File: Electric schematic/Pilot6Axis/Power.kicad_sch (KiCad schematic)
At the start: 14 parts, among them IC1 LM27313XMFX_NOPB, J1 Power switch, U1 AMS1117-3.3

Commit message: update schematic to kicajd 9.0,    fixed usb D=/D- wrongly inerconnected , otherwise pcb seems to be woekring
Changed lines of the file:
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@@
 (kicad_sch
-	(version 20231120)
+	(version 20250114)
 	(generator "eeschema")
-	(generator_version "8.0")
+	(generator_version "9.0")
 	(paper "A4")
 	(junction

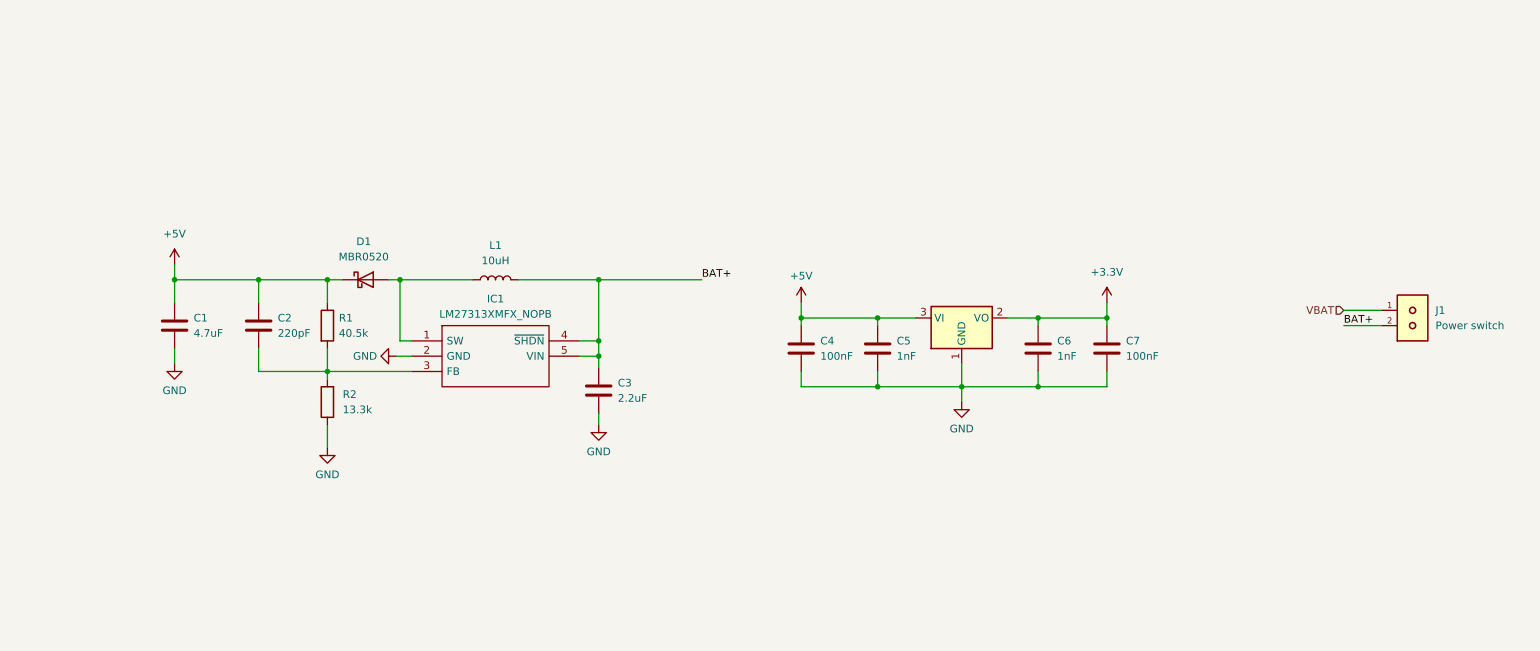
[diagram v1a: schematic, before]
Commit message: upgrade board to use USB BD for power delivery and addded SPI screen conector
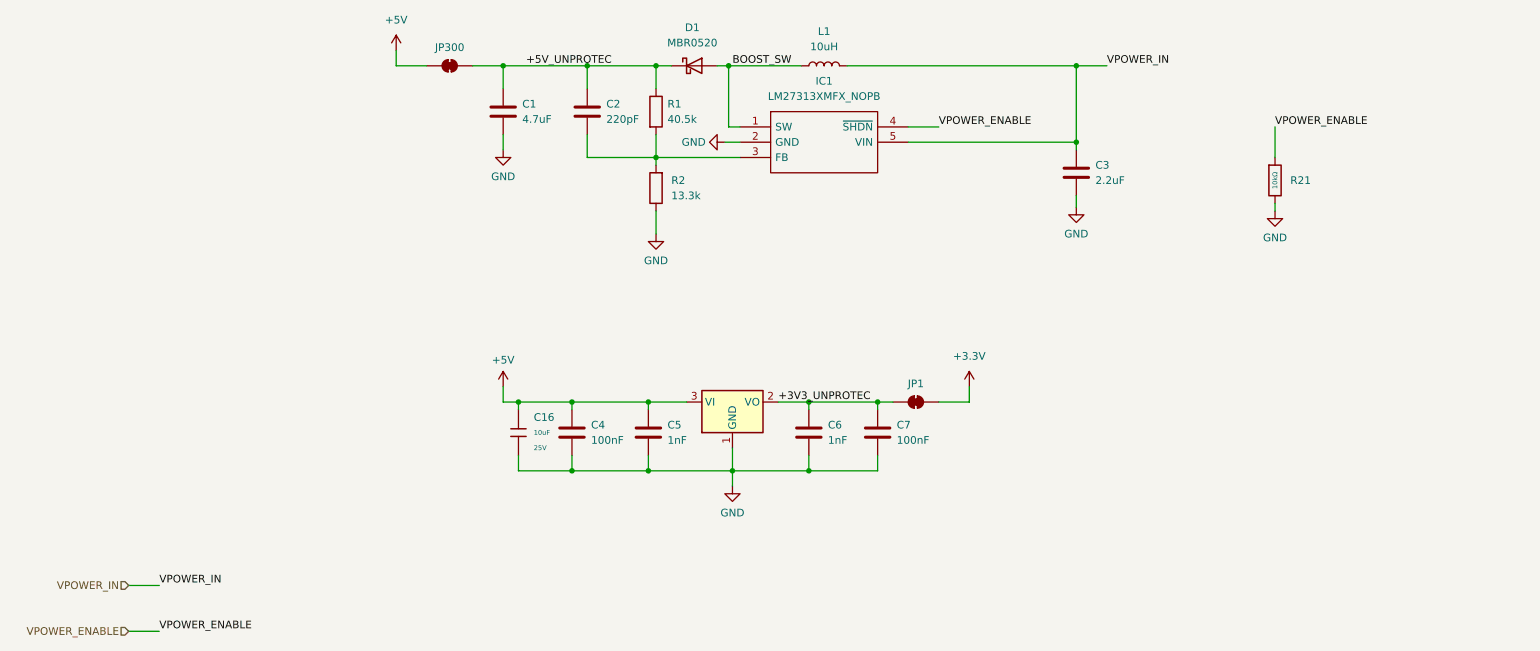
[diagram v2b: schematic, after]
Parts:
- removed J1: Power switch, Connector_Molex:Molex_KK-254_AE-6410-02A_1x02_P2.54mm_Vertical, symbol molex-2pin:22-27-2021
- added C16: 10uF, PCM_JLCPCB:C_0603, symbol PCM_JLCPCB-Capacitors:0603,10uF,(2)
- added JP1, JP300: SolderJumper_2_Bridged, Jumper:SolderJumper-2_P1.3mm_Open_TrianglePad1.0x1.5mm, symbol Jumper:SolderJumper_2_Bridged
- added R21: 10kΩ, PCM_JLCPCB:R_0603, symbol PCM_JLCPCB-Resistors:0603,10kΩ
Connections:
- net +3.3V: now also JP1.2 (B); no longer C6.1, C7.1, U1.2 (VO)
- net +5V: now also C16.1, JP300.1 (A); no longer C1.1, C2.2, D1.1 (K), R1.1
- net GND: now also C16.2, R21.2
- net BOOST_SW: now reaches D1.2 (A), IC1.1 (SW), L1.1
- net BAT+ renamed VPOWER_IN
- net VPOWER_IN: no longer IC1.4 (~{SHDN})
- new net +3V3_UNPROTEC: C6.1, C7.1, JP1.1 (A), U1.2 (VO)
- new net +5V_UNPROTEC: C1.1, C2.2, D1.1 (K), JP300.2 (B), R1.1
- new net VPOWER_ENABLE: IC1.4 (~{SHDN}), R21.1
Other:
- moved on the sheet: C1, C2, C3, C4, C5, C6, C7, D1, IC1, L1, R1, R2

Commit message: fixed leyout
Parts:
- removed C3: 2.2uF, Capacitor_SMD:C_0603_1608Metric, symbol Device:C
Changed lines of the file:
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@@
-	)
-	(junction
-		(at 200.66 72.39)
-		(diameter 0)
-		(color 0 0 0 0)
 	)
 	(junction
@@
 	)
 	(junction
+		(at 196.85 72.39)
+		(diameter 0)
+		(color 0 0 0 0)
+	)
+	(junction
 		(at 116.84 139.7)
 		(diameter 0)
@@
 	)
 	(junction
-		(at 200.66 85.09)
-		(diameter 0)
-		(color 0 0 0 0)
-	)
-	(junction
 		(at 105.41 72.39)
 		(diameter 0)
@@
 	(wire
 		(pts
-			(xy 200.66 85.09) (xy 172.72 85.09)
+			(xy 196.85 85.09) (xy 172.72 85.09)
 		)
 		(stroke
@@
 	(wire
 		(pts
-			(xy 200.66 72.39) (xy 200.66 85.09)
+			(xy 196.85 72.39) (xy 196.85 85.09)
 		)
 		(stroke
@@
 	(wire
 		(pts
-			(xy 162.56 72.39) (xy 200.66 72.39)
+			(xy 162.56 72.39) (xy 196.85 72.39)
 		)
 		(stroke
@@
 	(wire
 		(pts
-			(xy 200.66 72.39) (xy 205.74 72.39)
-		)
-		(stroke
-			(width 0)
-			(type default)
-		)
-	)
-	(wire
-		(pts
 			(xy 151.13 128.27) (xy 156.21 128.27)
 		)
@@
 	(wire
 		(pts
-			(xy 200.66 93.98) (xy 200.66 95.885)
+			(xy 196.85 72.39) (xy 205.74 72.39)
 		)
 		(stroke
@@
 		(pts
 			(xy 154.94 72.39) (xy 142.875 72.39)
-		)
-		(stroke
-			(width 0)
-			(type default)
-		)
-	)
-	(wire
-		(pts
-			(xy 200.66 85.09) (xy 200.66 86.36)
 		)
 		(stroke
@@
 	)
 	(symbol
-		(lib_id "power:GND")
-		(at 200.66 95.885 0)
-		(unit 1)
-		(exclude_from_sim no)
-		(in_bom yes)
-		(on_board yes)
-		(dnp no)
-		(fields_autoplaced yes)
-		(property "Reference" "#PWR05"
-			(at 200.66 102.235 0)
-			(effects
-				(font
-					(size 1.27 1.27)
-				)
-				(hide yes)
-			)
-		)
-		(property "Value" "GND"
-			(at 200.66 100.33 0)
-			(effects
-				(font
-					(size 1.27 1.27)
-				)
-			)
-		)
-		(property "Footprint" ""
-			(at 200.66 95.885 0)
-			(effects
-				(font
-					(size 1.27 1.27)
-				)
-				(hide yes)
-			)
-		)
-		(property "Datasheet" ""
-			(at 200.66 95.885 0)
-			(effects
-				(font
-					(size 1.27 1.27)
-				)
-				(hide yes)
-			)
-		)
-		(property "Description" ""
-			(at 200.66 95.885 0)
-			(effects
-				(font
-					(size 1.27 1.27)
-				)
-				(hide yes)
-			)
-		)
-		(pin "1"
-		)
-		(instances
-			(project "Pilot6Axis"
-				(path "/085b8362-a5df-4186-a09b-4280628dd4a5/504d928c-edb5-470d-96cf-de0a899dce19"
-					(reference "#PWR05")
-					(unit 1)
-				)
-			)
-		)
-	)
-	(symbol
 		(lib_id "Device:C")
 		(at 129.54 133.35 0)
@@
 					(unit 1)
 				)
-			)
-		)
-	)
-	(symbol
-		(lib_id "Device:C")
-		(at 200.66 90.17 0)
-		(unit 1)
-		(exclude_from_sim no)
-		(in_bom yes)
-		(on_board yes)
-		(dnp no)
-		(fields_autoplaced yes)
-		(property "Reference" "C3"
-			(at 203.835 88.9 0)
-			(effects
-				(font
-					(size 1.27 1.27)
-				)
-				(justify left)
-			)
-		)
-		(property "Value" "2.2uF"
-			(at 203.835 91.44 0)
-			(effects
-				(font
-					(size 1.27 1.27)
-				)
-				(justify left)
-			)
-		)
-		(property "Footprint" "Capacitor_SMD:C_0603_1608Metric"
-			(at 201.6252 93.98 0)
-			(effects
-				(font
-					(size 1.27 1.27)
-				)
-				(hide yes)
-			)
-		)
-		(property "Datasheet" "~"
-			(at 200.66 90.17 0)
-			(effects
-				(font
-					(size 1.27 1.27)
-				)
-				(hide yes)
-			)
-		)
-		(property "Description" ""
-			(at 200.66 90.17 0)
-			(effects
-				(font
-					(size 1.27 1.27)
-				)
-				(hide yes)
-			)
-		)
-		(property "LCSC" "C23630"
-			(at 203.835 88.9 0)
-			(effects
-				(font
-					(size 1.27 1.27)
-				)
-				(hide yes)
-			)
-		)
-		(pin "2"
-		)
-		(pin "1"
-		)
-		(instances
-			(project "Pilot6Axis"
-				(path "/085b8362-a5df-4186-a09b-4280628dd4a5/504d928c-edb5-470d-96cf-de0a899dce19"
-					(reference "C3")
-					(unit 1)
-				)
